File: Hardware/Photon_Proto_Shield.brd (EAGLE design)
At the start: 40.6 x 35.6 mm, 14 parts

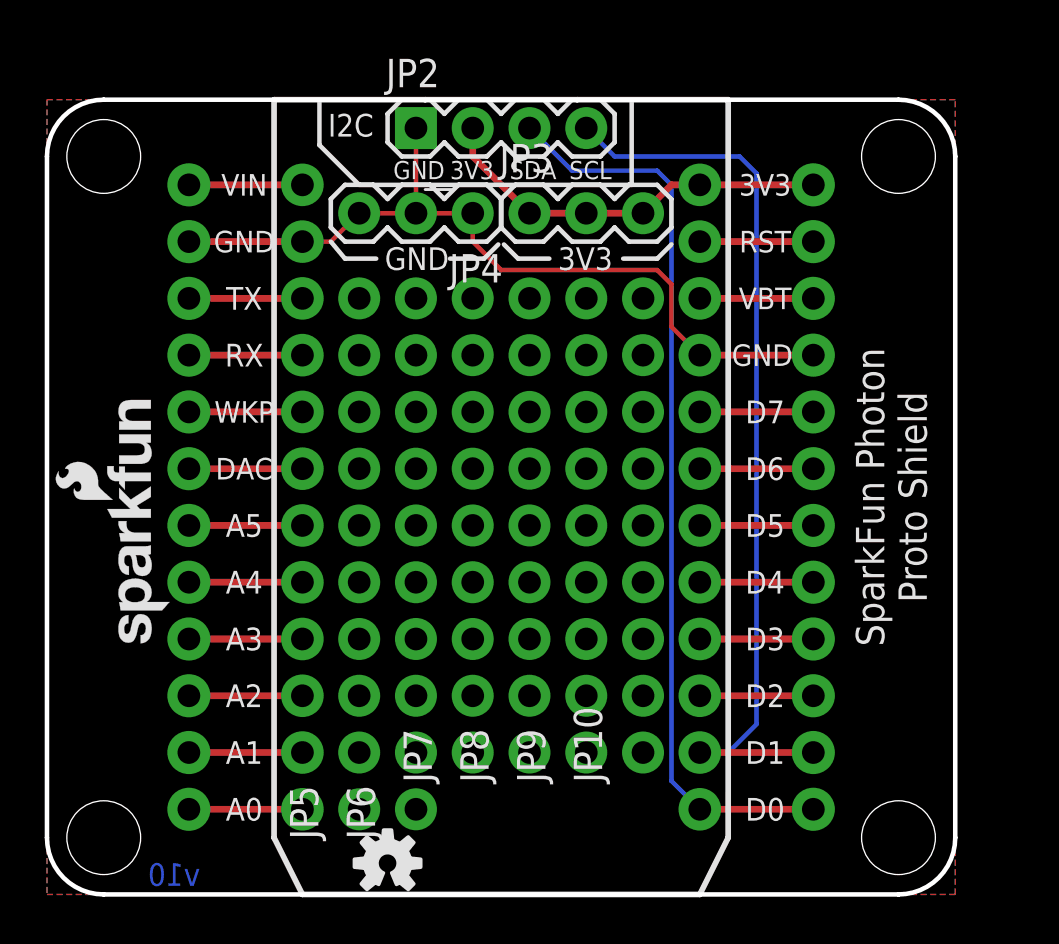
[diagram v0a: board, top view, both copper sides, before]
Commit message: Bottom-lefting origin. Revising board name.
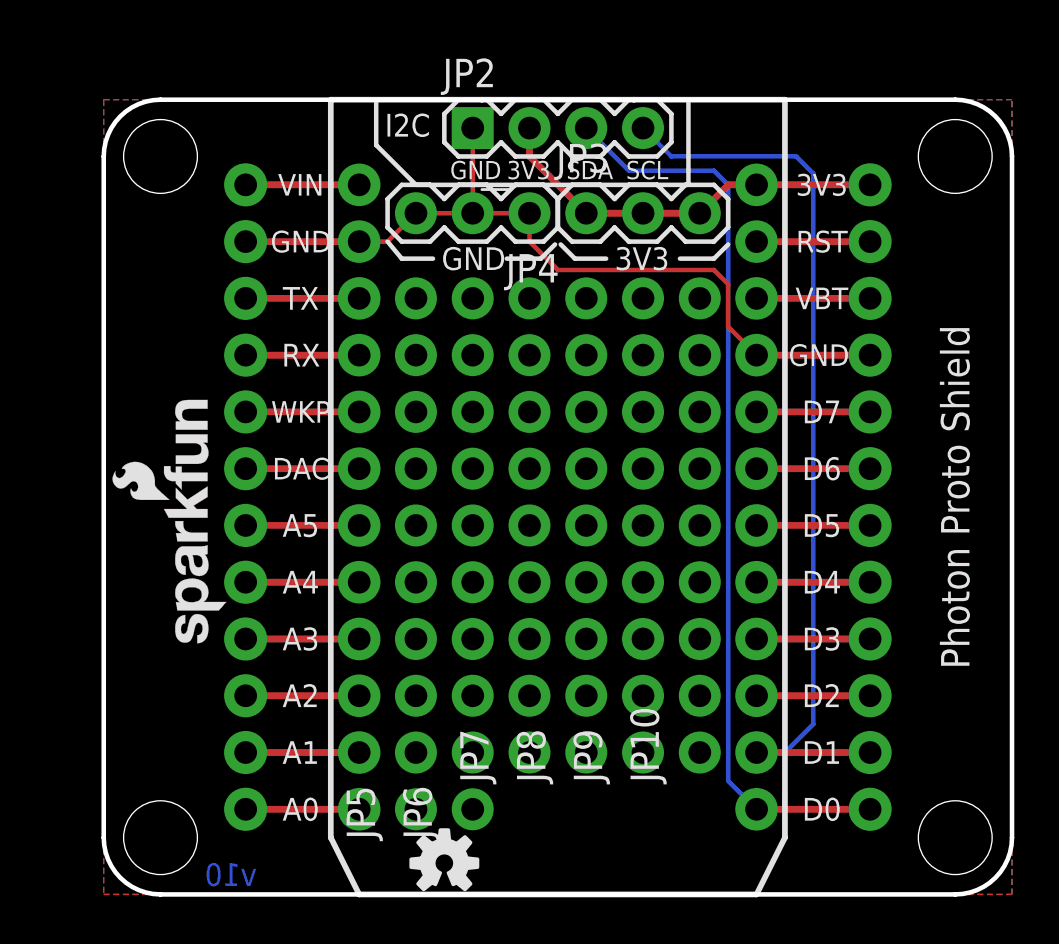
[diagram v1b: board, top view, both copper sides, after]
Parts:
- moved JP10 2.54 mm to (26.7, 6.35)
- moved JP2 2.54 mm to (16.5, 34.3)
- moved JP5 2.54 mm to (14.0, 3.81)
- moved JP6 2.54 mm to (16.5, 3.81)
- moved LOGO2 2.54 mm to (15.2, 1.40)
- moved JP1 2.54 mm to (10.2, 0.00)
- moved LOGO1 2.54 mm to (5.59, 10.8)
- moved LOGO3 2.54 mm to (5.59, 22.6)
- moved JP3 2.54 mm to (21.6, 30.5)
- moved JP4 2.54 mm to (19.1, 30.5)
- moved JP7 2.54 mm to (19.1, 6.35)
- moved JP8 2.54 mm to (21.6, 6.35)
- moved JP9 2.54 mm to (24.1, 6.35)
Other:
- board text added: "Photon Proto Shield"
- board text added: "Units in Inches"
- board text removed: "SparkFun Photon Proto Shield"
